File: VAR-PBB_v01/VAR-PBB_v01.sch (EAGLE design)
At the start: 20 parts, among them J1 ANDERSON_POWER_POLE, J11 CON1X2_SHROUDED, J2 ANDERSON_POWER_POLE, J3 CON1X2_SHROUDED, J4 CON1X2_SHROUDED, J5 CON1X2_SHROUDED, J6 CON1X2_SHROUDED, J7 CON1X2_SHROUDED, J8 CON1X2_SHROUDED, U1 OKI-78SR, U2 XL6009, U3 XL6009, U4 XL6009

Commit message: WIP, but got a ton done.
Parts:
- added C1, C4, C5: 0.1uF, SparkFun-Capacitors:0.1UF-0603-25V-5%
- added C2: 1.0uF, SparkFun-Capacitors:1.0UF-0603-16V-10%
- added C3: 2.2uF, SparkFun-Capacitors:2.2UF-0603-10V-20%
- added R1, R2, R3: (no value), SparkFun-Resistors:RESISTOR0603
- added U5: LP2985AIM5-1.5, LP2985AIM5-1.5:LP2985AIM5-1.5
- added U6: TPS259271DRCR, TPS259271DRCR:TPS259271DRCR
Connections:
- removed net N$6: J10.1
- new net 1.5V_REG: C3.1, J10.1, U5.OUT
- new net N$12: R3.2, U6.ILIM
- new net N$13: C5.2, U6.EN/UVLO
- new net N$14: R1.1, R2.2, U6.DV/DT
- new net N$8: C1.1, U5.CBYP
- net BATT+: now also C2.1, C4.2, U5.IN, U5.ON/~OFF, U6.OUT, U6.OUT_2, U6.OUT_3
- net GND: now also C1.2, C2.2, C3.2, C4.1, C5.1, R2.1, R3.1, U5.GND, U6.EPAD
- net N$1: now also R1.2, U6.VIN, U6.VIN_2, U6.VIN_3
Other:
- note removed: "Use E-fuse?"
- moved on the sheet: J1, S1

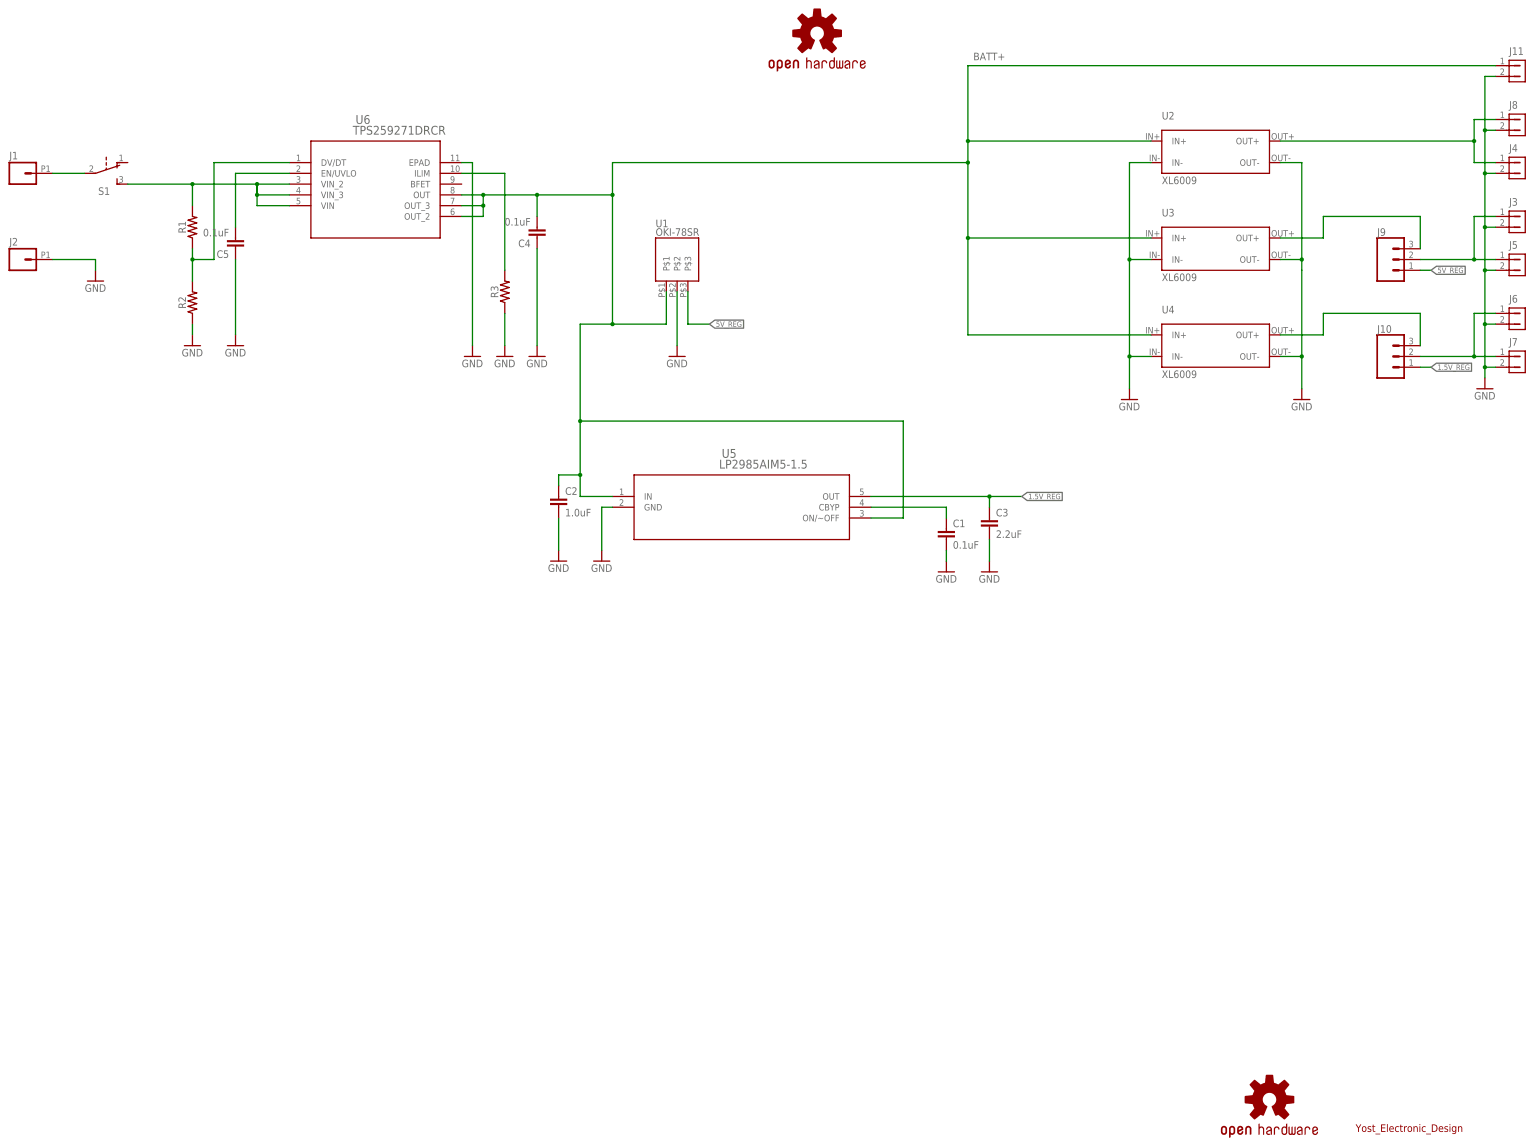
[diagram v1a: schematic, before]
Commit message: Got all of the features in, board layout done, silk screen tweaked. Need to pick resistor values for UVLO and dV/dT, power LED, and finish BOM xls.
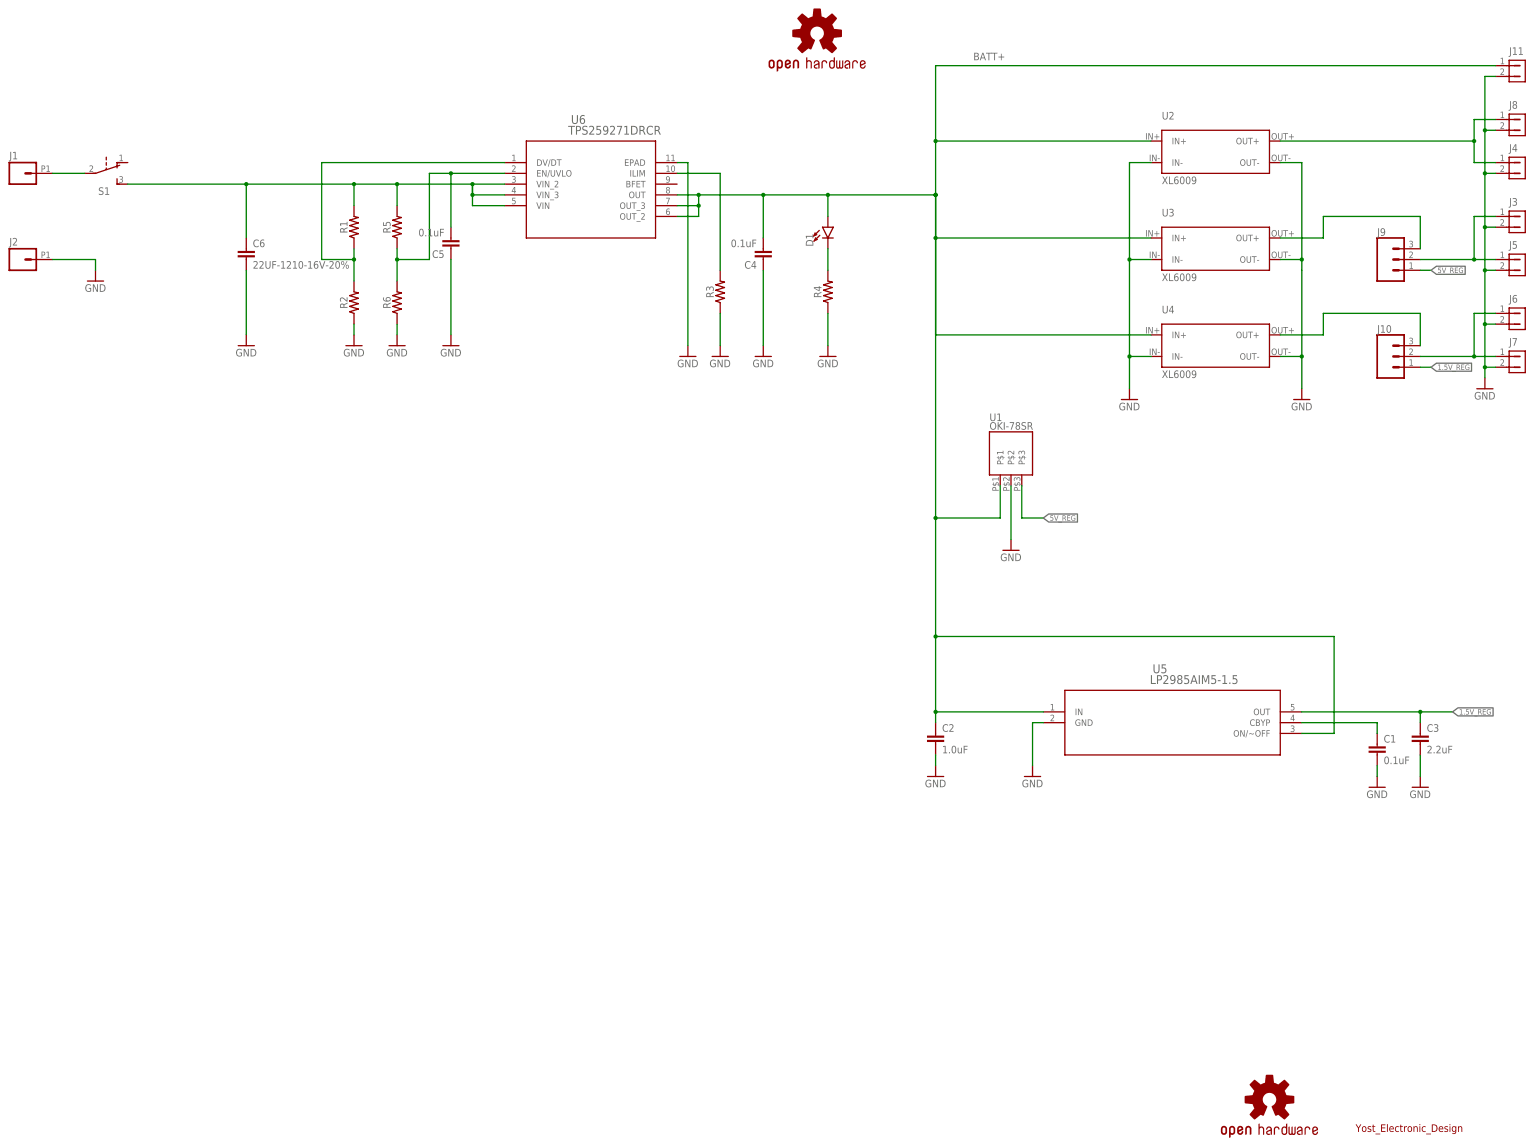
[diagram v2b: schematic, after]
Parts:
- added C6: 22UF-1210-16V-20%, SparkFun-Capacitors:22UF-1210-16V-20%
- added D1: (no value), SparkFun-LED:LED5MM
- added R4, R5, R6: (no value), SparkFun-Resistors:RESISTOR0603
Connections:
- removed net N$13: C5.2, U6.EN/UVLO
- new net N$2: D1.C, R4.2
- new net N$4: C5.2, R5.1, R6.2, U6.EN/UVLO
- net BATT+: now also D1.A
- net GND: now also C6.2, R4.1, R6.1
- net N$1: now also C6.1, R5.2
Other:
- moved on the sheet: C1, C2, C3, C4, C5, R1, R2, R3, U1, U5, U6

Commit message: v01 done - schematic complete and cleaned up, board fully routed, passes DRC, BOM complete.
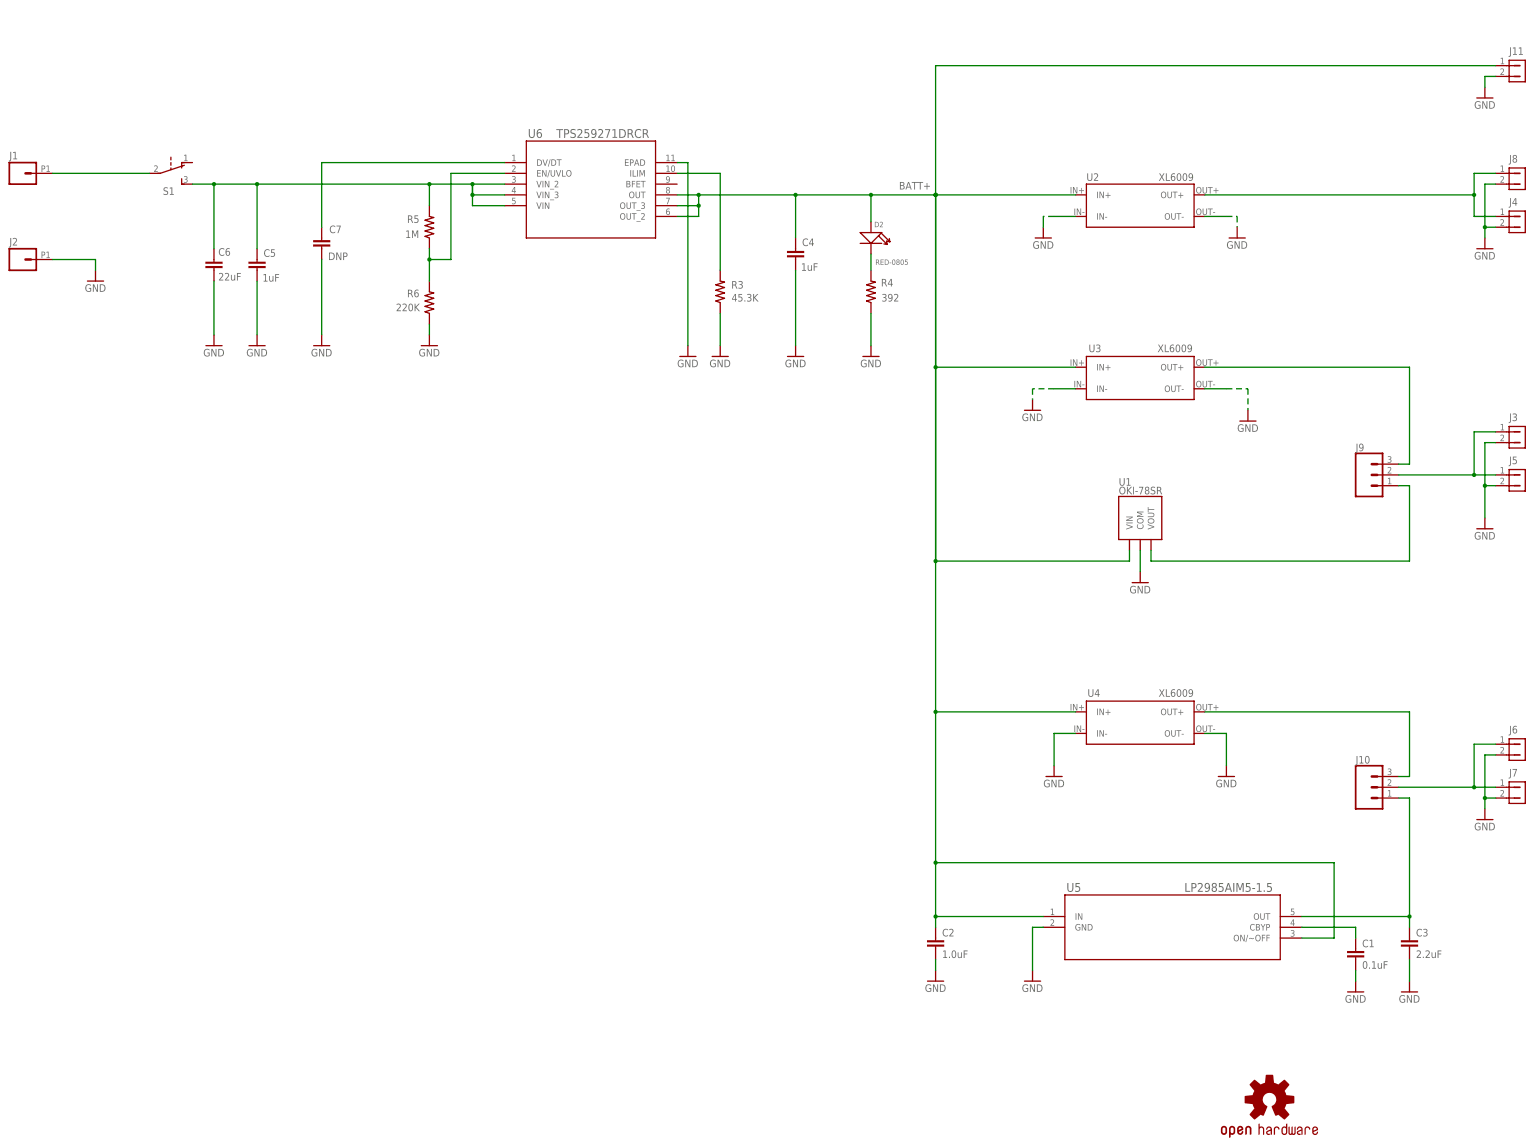
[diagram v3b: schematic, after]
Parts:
- removed D1: (no value), SparkFun-LED:LED5MM
- removed LOGO1: OSHW-LOGOM, SparkFun-Aesthetics:OSHW-LOGOM
- removed R1, R2: (no value), SparkFun-Resistors:RESISTOR0603
- removed U$5: ROHS_GARBAGE, SchmalzHausPublic:ROHS_GARBAGE
- added C7: DNP, SparkFun-Capacitors:0.1UF-0603-25V-5%
- added D2: RED-0805, OPL_Optoelectronics:SMD-LED-CLEAR-RED(0805)
- C4, C5: value 0.1uF -> 1uF
- C6: value 22UF-1210-16V-20% -> 22uF
- R3: value (none) -> 45.3K
- R4: value (none) -> 392
- R5: value (none) -> 1M
- R6: value (none) -> 220K
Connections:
- net 5V_REG: now also U1.VOUT; no longer U1.P$3
- net BATT+: now also D2.+, U1.VIN; no longer D1.A, U1.P$1
- net GND: now also C7.1, U1.COM; no longer R2.1, U1.P$2
- net N$1: now also C5.2; no longer R1.2
- net N$14: now also C7.2; no longer R1.1, R2.2
- net N$2: now also D2.-; no longer D1.C
- net N$4: no longer C5.2
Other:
- note added: "1%"
- note added: "1.5V Fixed Regualtor"
- note added: "1.5V Outputs"
- note added: "1210 16V"
- note added: "5V Fixed Regulator"
- note added: "5V Outputs"
- note added: "Battery input power 5V to 18V (9.6V typical - NiMH)"
- note added: "Copyright 2019 Engineering^3 LLC Copyright and related rights are licensed under the Solderpad Hardware License, Version 0.51 (the “License”); you may not use this file except in compliance with the License. You may obtain a copy of the License at http://solderpad.org/licenses/SHL-0.51. Unless required by applicable law or agreed to in writing, software, hardware and materials distributed under t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"
- note added: "Copyright 2020 Engineering^3 LLC"
- note added: "Designed for Tim Jump of Engineering^3 by Brian Schmalz of Schmalz Haus LLC"
- note added: "E-Fuse Provides: - Undervoltage Lock Out (UVLO) (8V default) - Over Current Protection (Set to 2.1A max)"
- note added: "Fixed 1.5V (default)"
- note added: "Fixed 5V (default)"
- note added: "Optional Variable Regulator for J3/J5"
- note added: "Optional Variable Regulator for J6/J7"
- note added: "Power LED"
- note added: "Power LED will turn off if any of the following is true: - Power switch is off - Battery voltage is too low (needs charging) - Over current fault detected"
- note added: "Power Switch"
- note added: "RED"
- note added: "Raw Battery Output Voltage will be whatever voltage the battery is outputting"
- note added: "VAR_PBB v01 Variable Power Board"
- note added: "Variable Outputs (1.25V - 35V) Max current depends on voltage."
- note added: "Variable Regulator (nom. 12V) Settable from 1.25 to 35V"
- note removed: "1.5V Output"
- note removed: "5V Output"
- note removed: "Copyright 2016 Engineering^3 LLC"
- note removed: "Copyright 2016 Engineering^3 LLC Copyright and related rights are licensed under the Solderpad Hardware License, Version 0.51 (the “License”); you may not use this file except in compliance with the License. You may obtain a copy of the License at http://solderpad.org/licenses/SHL-0.51. Unless required by applicable law or agreed to in writing, software, hardware and materials distributed under t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"
- note removed: "Fixed 5V"
- note removed: "Raw Battery Output"
- note removed: "Variable Output (1.25V - 35V) Max current depends on voltage."
- note removed: "Yost_Electronic_Design"
- moved on the sheet: C1, C2, C3, C4, C5, C6, J10, J3, J4, J5, J6, J7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
